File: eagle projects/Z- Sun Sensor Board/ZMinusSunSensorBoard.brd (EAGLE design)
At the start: 91 x 91 mm, 204 parts, among them J1 TE-1734829-2, J2 832-10-012-10-005000, J4 830-10-006-20-005000, J5 830-10-006-20-005000, J6 830-10-006-20-005000, J7 830-10-006-20-005000, U1 ADS7841E_2K5, U10 TSV991AILT, U11 TSV991AILT, U12 TSV991AILT, U13 ADS7841E_2K5, U14 TSV991AILT, U16 TSV991AILT, U17 TSV991AILT, U19 TSV991AILT, U2 ADS7841E_2K5, U21 TSV991AILT, U23 TSV991AILT, U25 ADS7841E_2K5, U26 TSV991AILT, U27 ADS7841E_2K5, U29 TSV991AILT, U3 TSV991AILT, U4 LM20BIM7X_NOPB, U5 LM20BIM7X_NOPB, U6 TSV991AILT, U8 TSV991AILT, U9 TSV991AILT

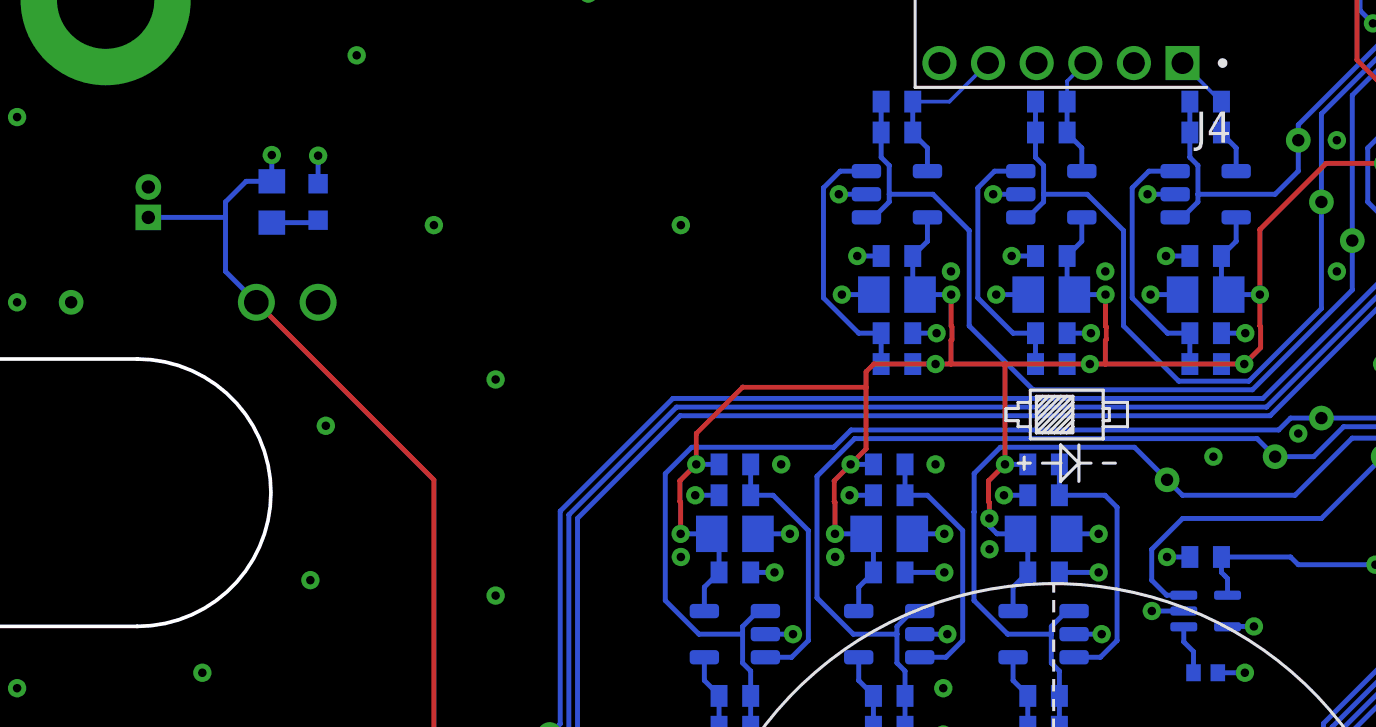
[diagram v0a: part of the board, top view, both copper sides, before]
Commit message: Removed LED to Z-
Removed a voltage testing LED and associated resistor from the Z- board, BOM was updated accordingly.
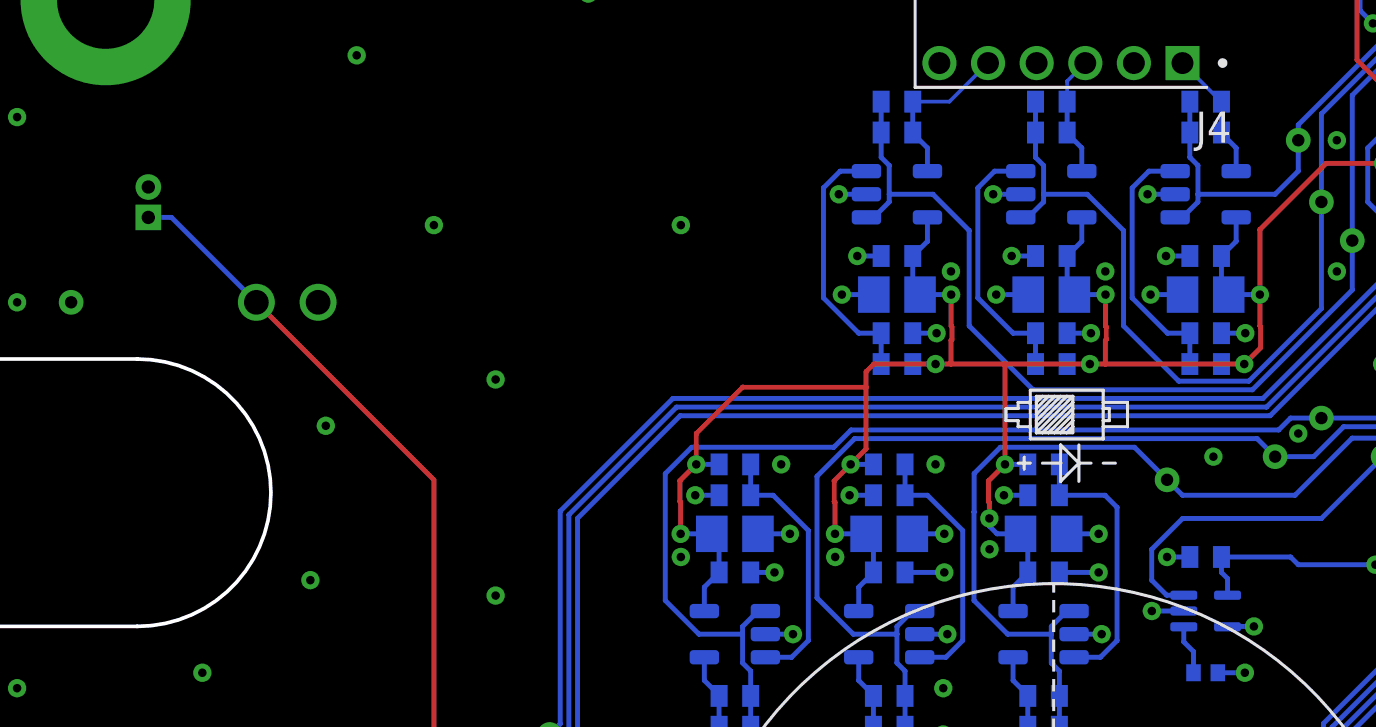
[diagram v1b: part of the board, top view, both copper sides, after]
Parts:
- removed LED1: (no value), led:CHIP-LED0603
- removed R11: (no value), rcl:R0603
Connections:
- removed net N$21: LED1.A, R11.1
- net +3V3: no longer R11.2
- net GND: no longer LED1.C
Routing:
- net +3V3: track 510.1 -> 504.8 mm, vias 55 -> 54
- net N$21: track 1.95 -> 0.00 mm
- net GND: track 140.0 -> 138.8 mm, vias 220 -> 219

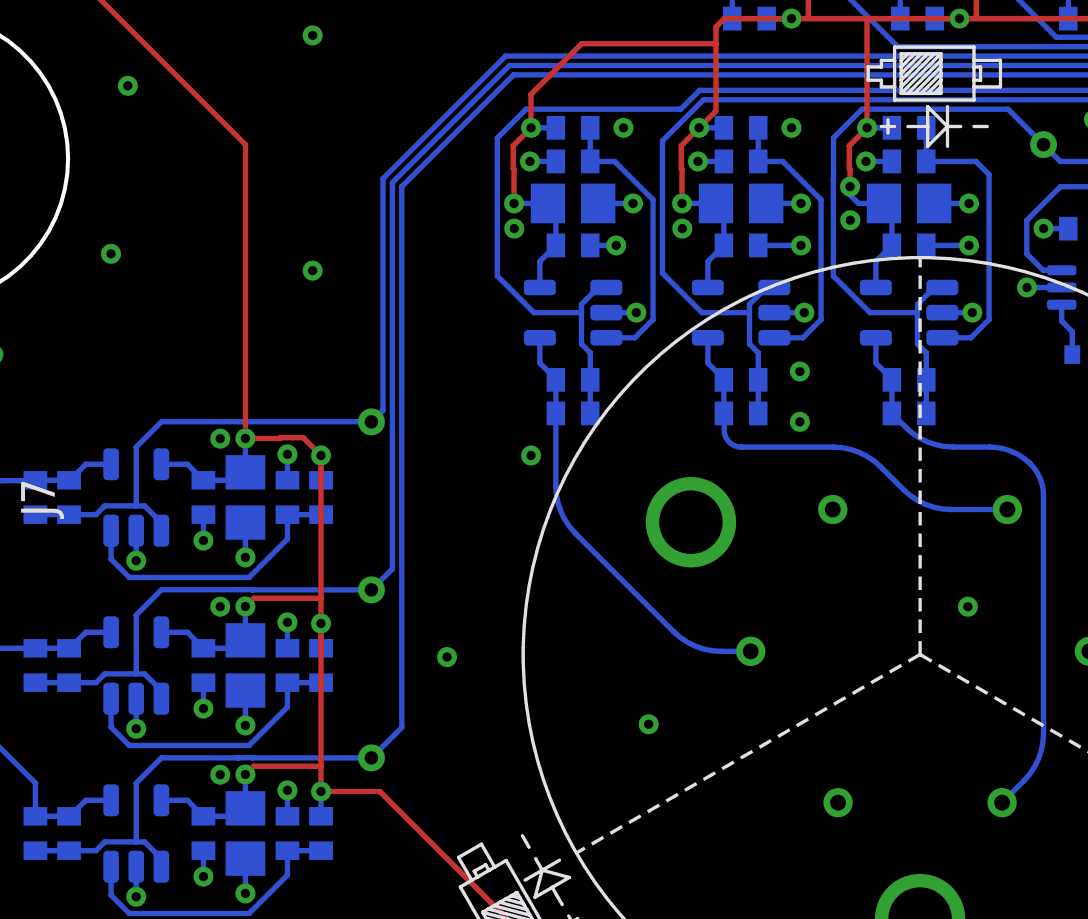
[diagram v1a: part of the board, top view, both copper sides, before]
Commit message: Air wires and wire stubs fixed on all boards
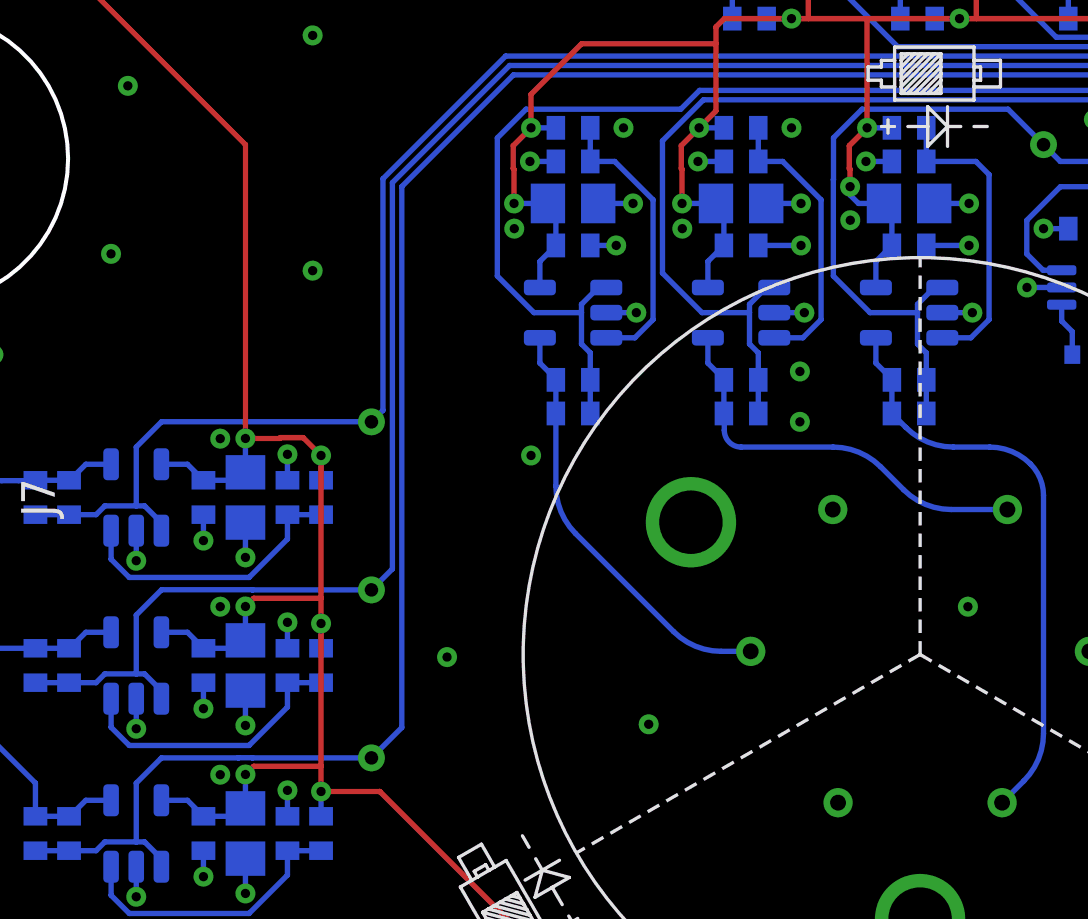
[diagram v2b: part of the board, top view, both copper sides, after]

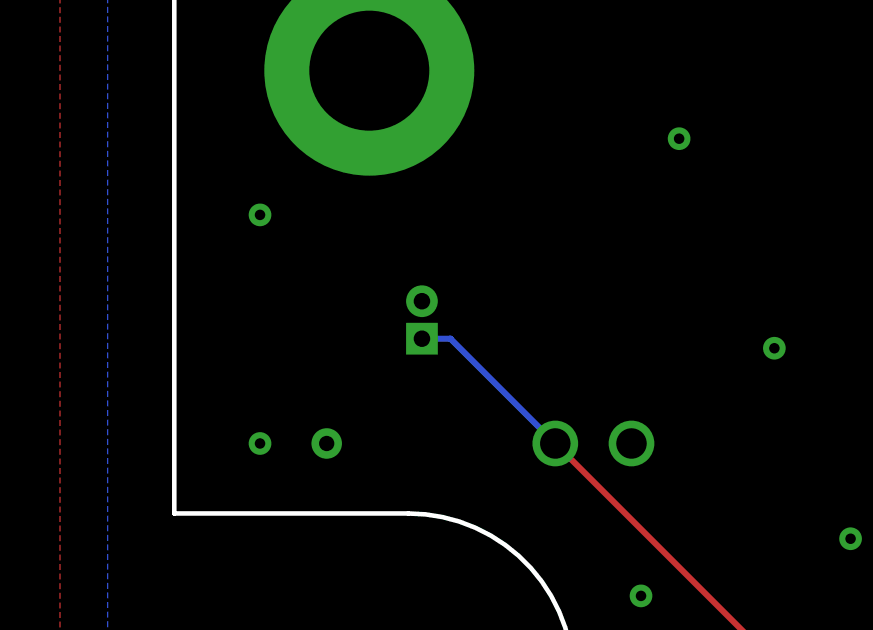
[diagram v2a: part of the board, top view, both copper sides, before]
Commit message: Added Luc's recommended new power connectors
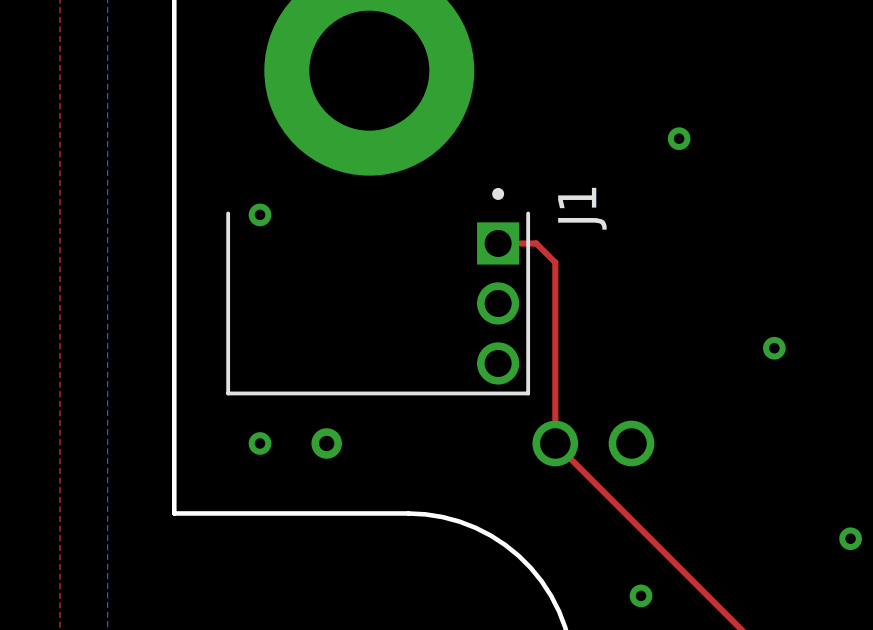
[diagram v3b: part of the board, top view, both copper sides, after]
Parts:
- J1: value TE-1734829-2 -> 830-10-003-20-005000; device my_library:TE-1734829-2 -> 830-10-003-20-005000:830-10-003-20-005000
- moved J1 4.07 mm to (10.8, 78.7), flipped to the top
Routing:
- net +3V3: track 504.8 -> 507.1 mm
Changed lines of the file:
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@@
 <element name="U$4" library="my_library" library_urn="urn:adsk.eagle:library:22876504" package="PHOTODIODE_SILK" value="" x="30.41514375" y="36.305059375" locked="yes" smashed="yes" rot="R300"/>
 <element name="U$5" library="my_library" library_urn="urn:adsk.eagle:library:22876504" package="PHOTODIODE_SILK" value="" x="60.966615625" y="36.494215625" locked="yes" smashed="yes" rot="R60"/>
-<element name="J1" library="my_library" library_urn="urn:adsk.eagle:library:22876504" package="TE-1734829-2" package3d_urn="urn:adsk.eagle:package:27602902/2" value="TE-1734829-2" x="8.255" y="75.565" smashed="yes" rot="MR270">
-<attribute name="NAME" x="9.525" y="79.375" size="1.27" layer="26" rot="MR180"/>
-</element>
 <element name="J3" library="my_library" library_urn="urn:adsk.eagle:library:22876504" package="1X02" package3d_urn="urn:adsk.eagle:package:24527019/1" value="" x="13.97" y="72.0725" smashed="yes" rot="MR180">
 <attribute name="NAME" x="16.2687" y="69.1388" size="1.27" layer="26" ratio="10" rot="MR0"/>
@@
 <attribute name="PURCHASE-URL" value="https://pricing.snapeda.com/search/part/2355104-4/?ref=eda" x="81.915" y="73.66" size="1.778" layer="27" rot="R270" display="off"/>
 <attribute name="VALUE" x="76.915" y="75.66" size="1.27" layer="27" rot="R270"/>
+</element>
+<element name="J1" library="830-10-003-20-005000" package="830-10-003-20-005000" value="830-10-003-20-005000" x="10.795" y="78.74" smashed="yes" rot="R270">
+<attribute name="AVAILABILITY" value="In Stock" x="10.795" y="78.74" size="1.778" layer="27" rot="R270" display="off"/>
+<attribute name="COMMENT" value="2355104-4" x="10.795" y="78.74" size="1.778" layer="27" rot="R270" display="off"/>
+<attribute name="DESCRIPTION" value=" Pin 4P,2MM,BRK HDR,SRVT,2.8,0.1AU,TB W/CAP 4 POS " x="10.795" y="78.74" size="1.778" layer="27" rot="R270" display="off"/>
+<attribute name="MF" value="TE Connectivity" x="10.795" y="78.74" size="1.778" layer="27" rot="R270" display="off"/>
+<attribute name="MP" value="2355104-4" x="10.795" y="78.74" size="1.778" layer="27" rot="R270" display="off"/>
+<attribute name="NAME" x="12.795" y="80.74" size="1.27" layer="25" rot="R270"/>
+<attribute name="PACKAGE" value="None" x="10.795" y="78.74" size="1.778" layer="27" rot="R270" display="off"/>
+<attribute name="PRICE" value="None" x="10.795" y="78.74" size="1.778" layer="27" rot="R270" display="off"/>
+<attribute name="PURCHASE-URL" value="https://pricing.snapeda.com/search/part/2355104-4/?ref=eda" x="10.795" y="78.74" size="1.778" layer="27" rot="R270" display="off"/>
+<attribute name="VALUE" x="-0.205" y="80.74" size="1.27" layer="27" rot="R270"/>
 </element>
 </elements>
@@
 <via x="59.0119" y="69.5325" extent="1-16" drill="0.35"/>
 <contactref element="J3" pad="1"/>
-<contactref element="J1" pad="1"/>
 <contactref element="C4" pad="1"/>
 <contactref element="R3" pad="2"/>
@@
 <wire x1="64.12" y1="70.8025" x2="64.4375" y2="70.485" width="0.2032" layer="16"/>
 <wire x1="52.6525" y1="60.71" x2="52.6525" y2="60.0225" width="0.2032" layer="16"/>
-<wire x1="9.2075" y1="75.565" x2="8.255" y2="75.565" width="0.2032" layer="16"/>
-<wire x1="12.7" y1="72.0725" x2="9.2075" y2="75.565" width="0.2032" layer="16"/>
+<contactref element="J1" pad="1"/>
+<wire x1="10.795" y1="78.74" x2="12.065" y2="78.74" width="0.2032" layer="1"/>
+<wire x1="12.065" y1="78.74" x2="12.7" y2="78.105" width="0.2032" layer="1"/>
+<wire x1="12.7" y1="78.105" x2="12.7" y2="72.0725" width="0.2032" layer="1"/>
 </signal>
 <signal name="GND">
@@
 <contactref element="U$1" pad="A2"/>
 <contactref element="U$1" pad="A3"/>
-<contactref element="J1" pad="2"/>
 <contactref element="J3" pad="2"/>
 <contactref element="U5" pad="2"/>
@@
 <via x="73.9775" y="8.5725" extent="1-16" drill="0.35"/>
 <via x="47.3075" y="47.3075" extent="1-16" drill="0.35"/>
+<contactref element="J1" pad="2"/>
 </signal>
 <signal name="UCB0_SPI_CLK">
